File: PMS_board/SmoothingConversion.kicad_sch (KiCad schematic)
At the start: 0 parts

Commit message: add microcontroller pinout
fixed hotswap, added pinouts to microcontroller, and made notes for power smoothing
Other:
- note added: "100A fuse"
- note added: "12V Buck"
- note added: "Bulk Capacitors"
- note added: "In Rush Protection"
- note added: "Pi filter"
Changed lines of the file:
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@@
 	(generator_version "10.0")
 	(paper "A4")
+	(text "Pi filter"
+		(exclude_from_sim no)
+		(at 45.72 68.326 0)
+		(effects
+			(font
+				(size 1.27 1.27)
+			)
+		)
+	)
+	(text "Bulk Capacitors\n"
+		(exclude_from_sim no)
+		(at 49.53 63.246 0)
+		(effects
+			(font
+				(size 1.27 1.27)
+			)
+		)
+	)
+	(text "In Rush Protection\n"
+		(exclude_from_sim no)
+		(at 51.054 58.674 0)
+		(effects
+			(font
+				(size 1.27 1.27)
+			)
+		)
+	)
+	(text "12V Buck "
+		(exclude_from_sim no)
+		(at 46.99 72.898 0)
+		(effects
+			(font
+				(size 1.27 1.27)
+			)
+		)
+	)
+	(text "100A fuse\n"
+		(exclude_from_sim no)
+		(at 46.99 77.724 0)
+		(effects
+			(font
+				(size 1.27 1.27)
+			)
+		)
+	)
 )

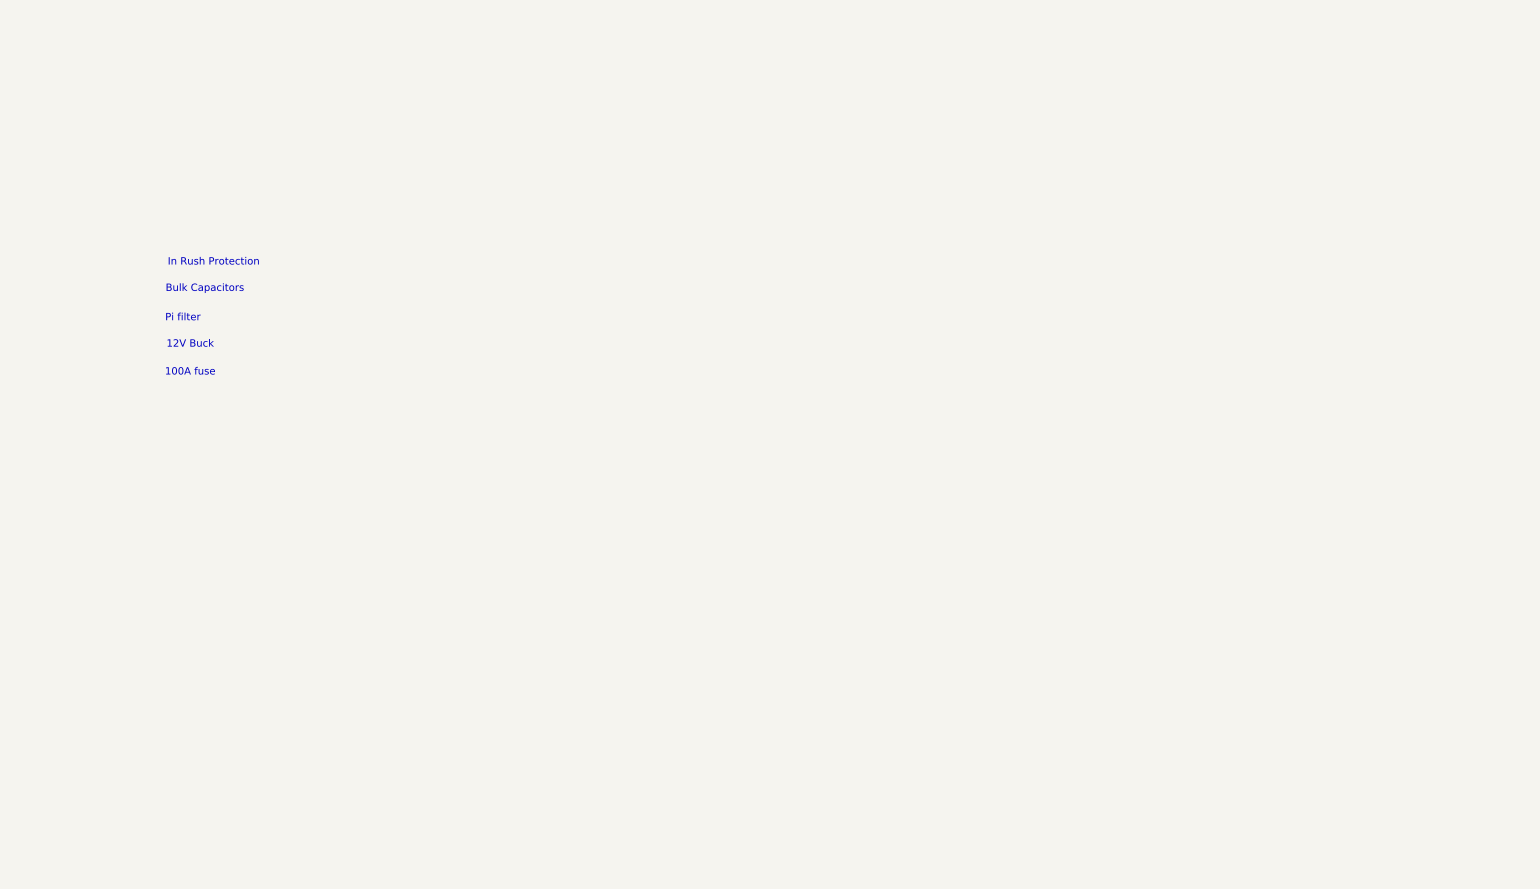
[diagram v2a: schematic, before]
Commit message: add power smoothing
I added the majority (i hope) of the necessary components for power smoothing and conversion. I also added notes to remind me and to inform others in my absence as to what still needs to be done to my knowledge.
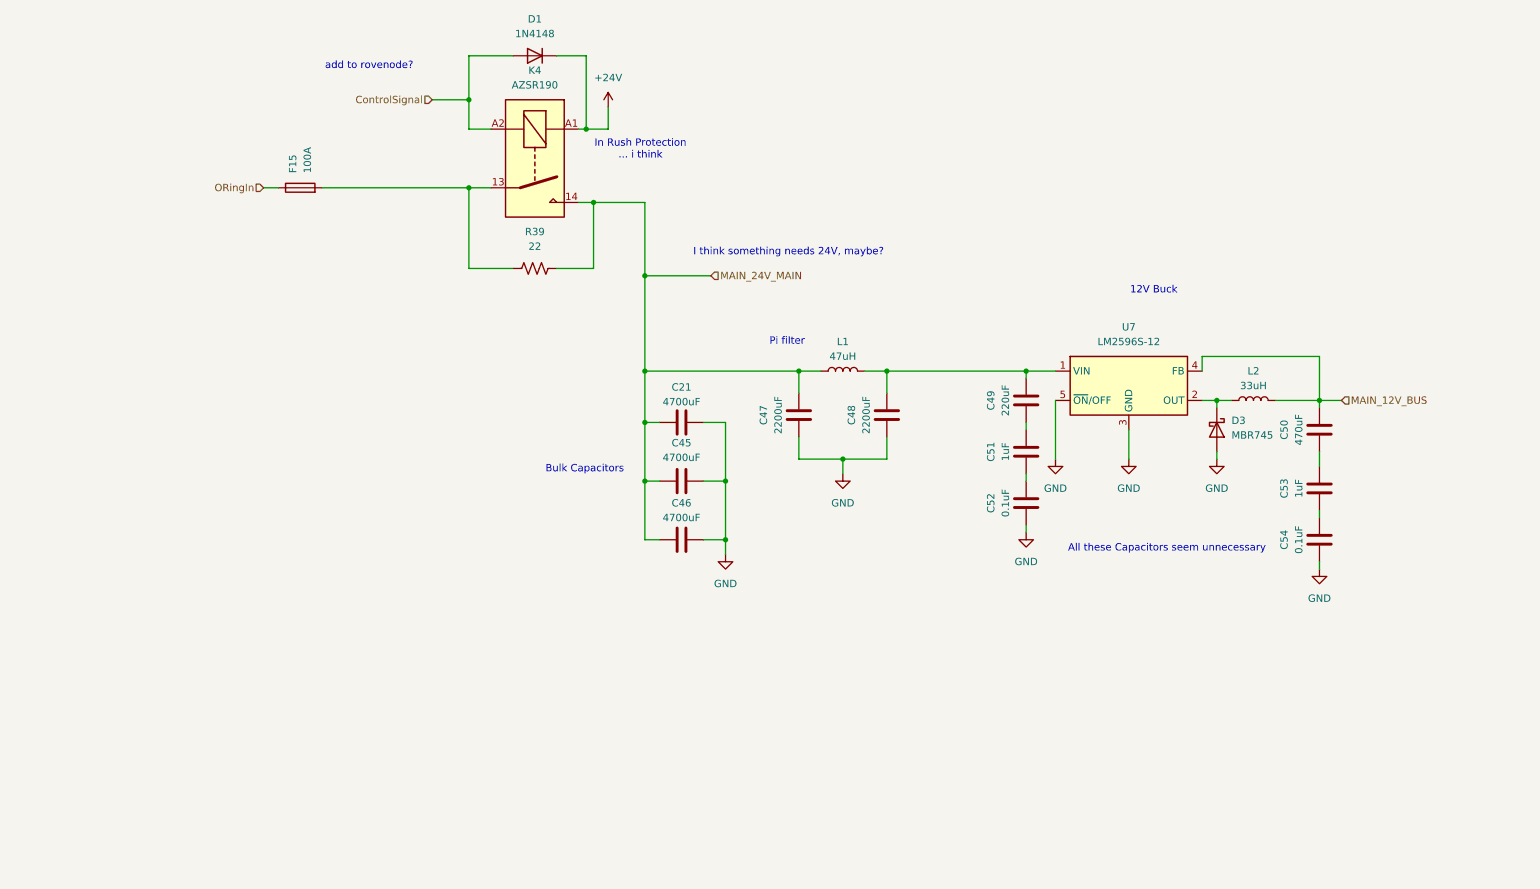
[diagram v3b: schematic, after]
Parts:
- added C21, C45, C46: 4700uF, symbol Device:C
- added C47, C48: 2200uF, symbol Device:C
- added C49: 220uF, symbol Device:C
- added C50: 470uF, symbol Device:C
- added C51, C53: 1uF, symbol Device:C
- added C52, C54: 0.1uF, symbol Device:C
- added D1: 1N4148, Diode_THT:D_DO-35_SOD27_P7.62mm_Horizontal, symbol Diode:1N4148
- added D3: MBR745, Package_TO_SOT_THT:TO-220-2_Vertical, symbol Diode:MBR745
- added F15: 100A, symbol Device:Fuse
- added K4: AZSR190, Relay_THT:Relay_SPST-NO_Fujitsu_FTR-LYAA005x_FormA_Vertical, symbol Relay:Relay_SPST-NO
- added L1: 47uH, symbol Device:L
- added L2: 33uH, symbol Device:L
- added R39: 22, symbol Device:R_US
- added U7: LM2596S-12, Package_TO_SOT_SMD:TO-263-5_TabPin3, symbol Regulator_Switching:LM2596S-12
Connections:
- new net: C50.2, C53.1
- new net: D3.1 (K), L2.1, U7.2 (OUT)
- new net: C53.2, C54.1
- new net: F15.2, K4.13, R39.2
- new net: C49.2, C51.1
- new net: C51.2, C52.1
- new net: C48.1, C49.1, L1.2, U7.1 (VIN)
- new net +24V: D1.1 (K), K4.A1
- new net ControlSignal: D1.2 (A), K4.A2
- new net GND: C21.1, C45.1, C46.1, C47.2, C48.2, C52.2, C54.2, D3.2 (A), U7.3 (GND), U7.5 (~{ON}/OFF)
- new net MAIN_12V_BUS: C50.1, L2.2, U7.4 (FB)
- new net MAIN_24V_MAIN: C21.2, C45.2, C46.2, C47.1, K4.14, L1.1, R39.1
- new net ORingIn: F15.1
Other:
- note added: "All these Capacitors seem unnecessary"
- note added: "I think something needs 24V, maybe?"
- note added: "In Rush Protection ... i think"
- note added: "add to rovenode?"
- note removed: "100A fuse"
- note removed: "In Rush Protection"

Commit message: add converter and friends
I added the converter symbols and updated the schematic. I chose the proper FETs and Diodes for ORing circuit.
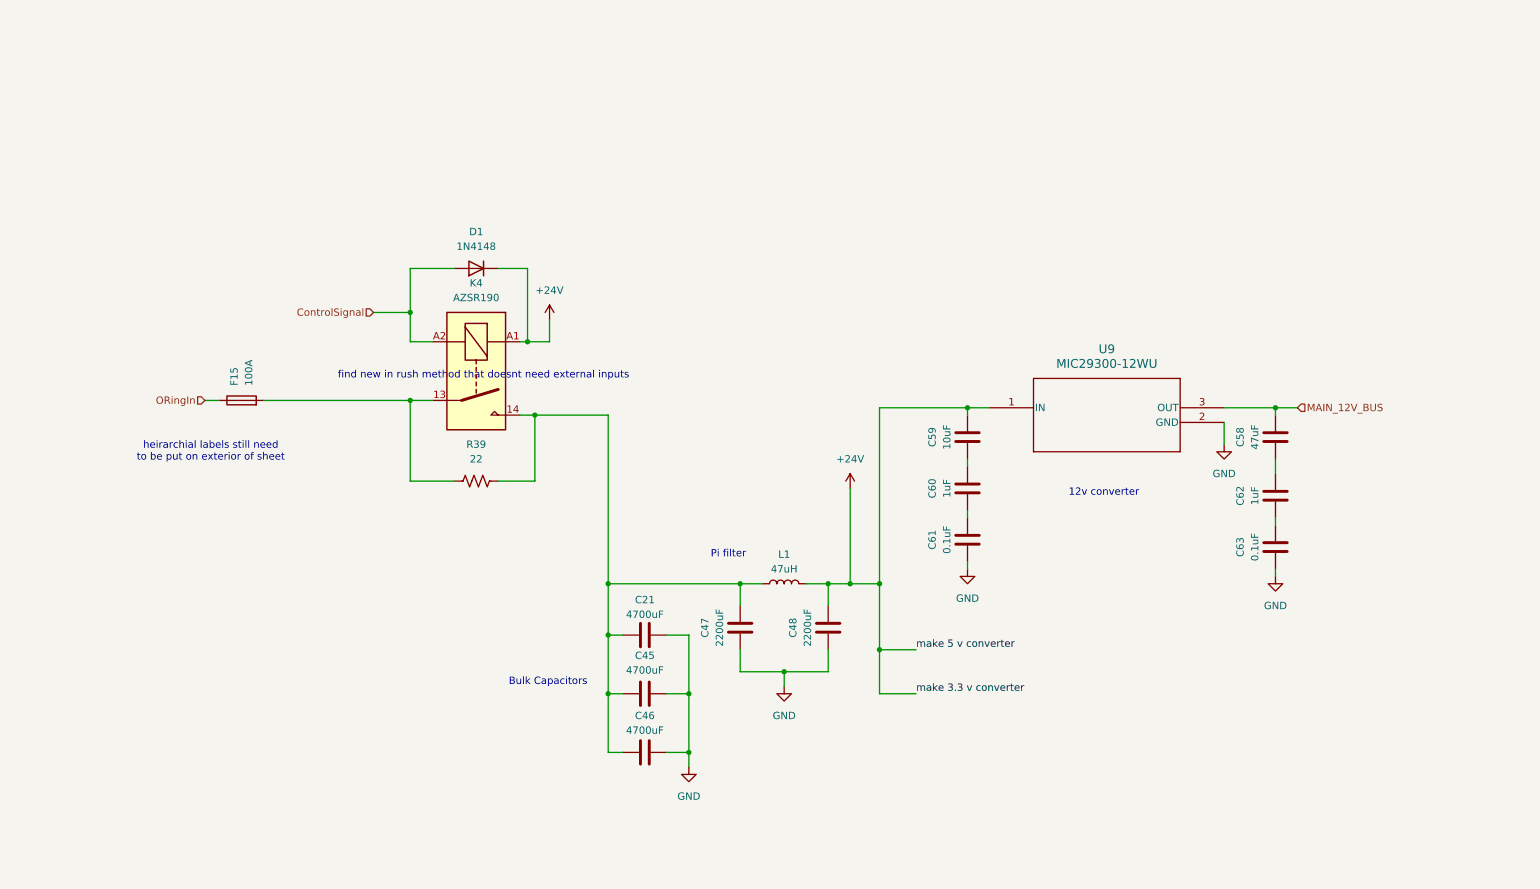
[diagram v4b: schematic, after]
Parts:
- removed C49: 220uF, symbol Device:C
- removed C50: 470uF, symbol Device:C
- removed C51, C53: 1uF, symbol Device:C
- removed C52, C54: 0.1uF, symbol Device:C
- removed D3: MBR745, Package_TO_SOT_THT:TO-220-2_Vertical, symbol Diode:MBR745
- removed L2: 33uH, symbol Device:L
- removed U7: LM2596S-12, Package_TO_SOT_SMD:TO-263-5_TabPin3, symbol Regulator_Switching:LM2596S-12
- added C58: 47uF, symbol Device:C
- added C59: 10uF, symbol Device:C
- added C60, C62: 1uF, symbol Device:C
- added C61, C63: 0.1uF, symbol Device:C
- added U9: MIC29300-12WU, TO220-3LD-PL-1_MCH, symbol MIC29300-12WU:MIC29300-12WU
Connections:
- net +24V: now also C48.1, L1.2, C59.1, U9.1 (IN)
- net GND: now also C61.2, C63.2, U9.2 (GND)
- net MAIN_12V_BUS: now also C58.1, U9.3 (OUT)
- net MAIN_24V_MAIN: no longer names the net of C21.2, C45.2, C46.2, C47.1, K4.14, L1.1, R39.1
- new net: C59.2, C60.1
- new net: C60.2, C61.1
- new net: C58.2, C62.1
- new net: C62.2, C63.1
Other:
- note added: "12v converter"
- note added: "find new in rush method that doesnt need external inputs"
- note added: "heirarchial labels still need to be put on exterior of sheet"
- note removed: "12V Buck"
- note removed: "All these Capacitors seem unnecessary"
- note removed: "I think something needs 24V, maybe?"
- note removed: "In Rush Protection ... i think"
- note removed: "add to rovenode?"
- moved on the sheet: C21, C45, C46, C47, C48, D1, F15, K4, L1, R39

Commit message: Add Bucks & Fix Issues
- Added 3V3 and 5V buck convertors
- Removed Pi filter
- adjusted capacitor values for Bulk Capacitors
- Added inrush protection to ORing circuit
- renamed various hierarchical pins for clarity
- renamed power rail pins due to naming conflicts
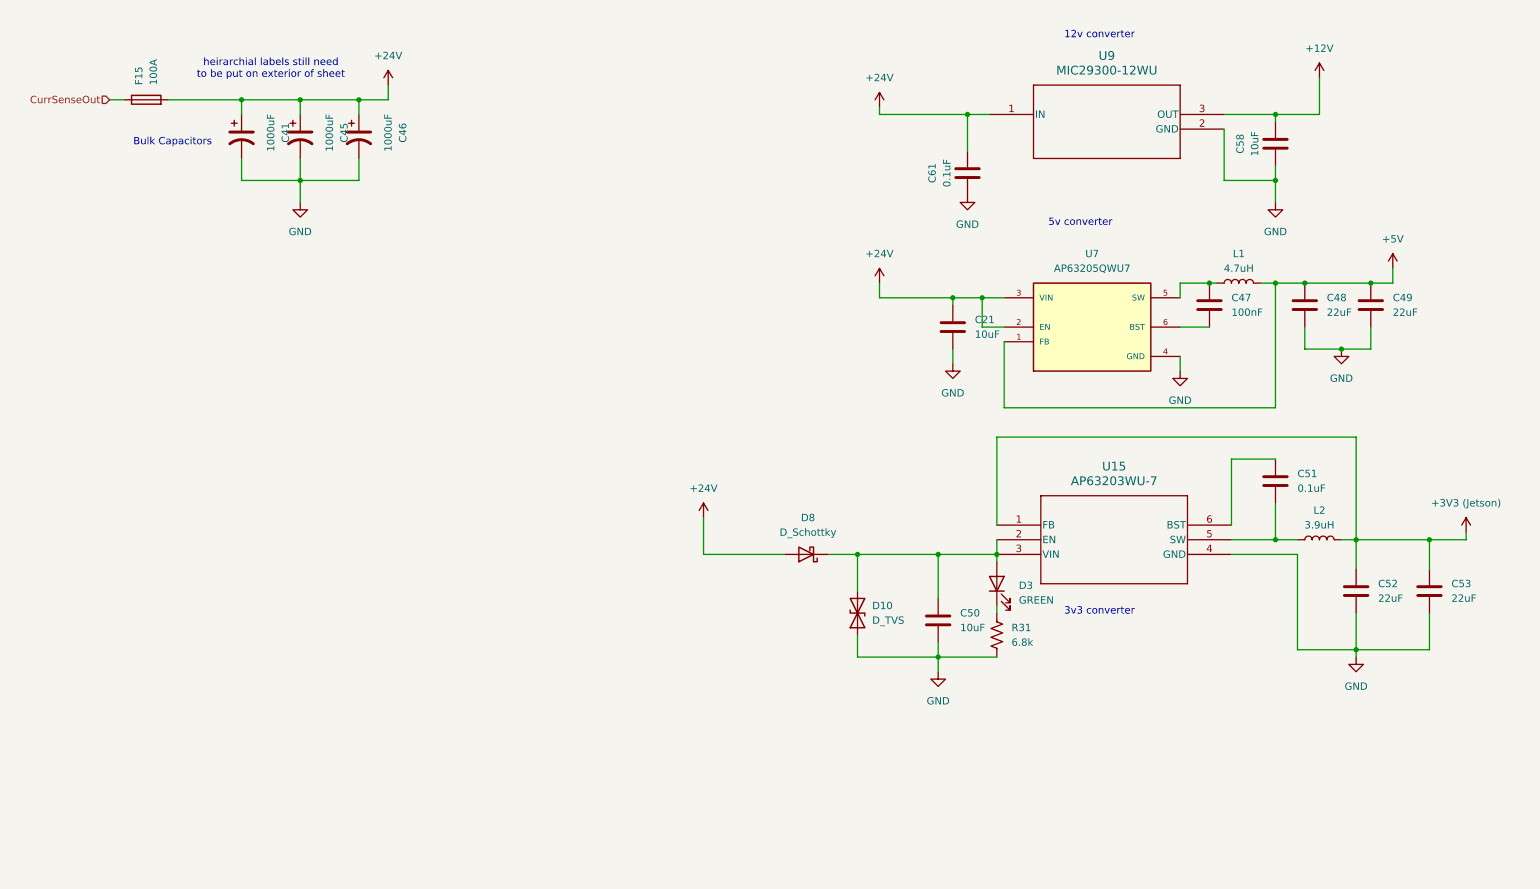
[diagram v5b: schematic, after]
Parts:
- removed C45, C46: 4700uF, symbol Device:C
- removed C59: 10uF, symbol Device:C
- removed C60, C62: 1uF, symbol Device:C
- removed C63: 0.1uF, symbol Device:C
- removed D1: 1N4148, Diode_THT:D_DO-35_SOD27_P7.62mm_Horizontal, symbol Diode:1N4148
- removed K4: AZSR190, Relay_THT:Relay_SPST-NO_Fujitsu_FTR-LYAA005x_FormA_Vertical, symbol Relay:Relay_SPST-NO
- removed R39: 22, symbol Device:R_US
- added C41, C45, C46: 1000uF, symbol Device:C_Polarized_US
- added C49: 22uF, Package_SO:SOIC-8_3.9x4.9mm_P1.27mm, symbol Device:C
- added C50: 10uF, Capacitor_SMD:C_0603_1608Metric_Pad1.08x0.95mm_HandSolder, symbol Device:C
- added C51: 0.1uF, Capacitor_SMD:C_0603_1608Metric_Pad1.08x0.95mm_HandSolder, symbol Device:C
- added C52, C53: 22uF, Capacitor_SMD:C_0603_1608Metric_Pad1.08x0.95mm_HandSolder, symbol Device:C
- added D10: D_TVS, Diode_SMD:D_SMA, symbol Device:D_TVS
- added D3: GREEN, LED_SMD:LED_0603_1608Metric_Pad1.05x0.95mm_HandSolder, symbol Device:LED
- added D8: D_Schottky, Diode_SMD:D_SOD-123F, symbol Device:D_Schottky
- added L2: 3.9uH, Inductor_SMD:L_1812_4532Metric_Pad1.30x3.40mm_HandSolder, symbol Device:L
- added R31: 6.8k, Resistor_SMD:R_0603_1608Metric_Pad0.98x0.95mm_HandSolder, symbol Device:R_US
- added U15: AP63203WU-7, SignalStack:AP63203WU-7_DIO, symbol AP63203WU-7:AP63203WU-7
- added U7: AP63205QWU7, AP63205QWU7:SOT95P280X100-6N, symbol AP63205QWU7:AP63205QWU7
- C21: value 4700uF -> 10uF; footprint (none) -> Package_SO:SOIC-8_3.9x4.9mm_P1.27mm
- C47: value 2200uF -> 100nF; footprint (none) -> Package_SO:SOIC-8_3.9x4.9mm_P1.27mm
- C48: value 2200uF -> 22uF; footprint (none) -> Package_SO:SOIC-8_3.9x4.9mm_P1.27mm
- C58: value 47uF -> 10uF
- L1: value 47uH -> 4.7uH; footprint (none) -> OptoDevice:Everlight_ITR9608-F
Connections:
- net +24V: now also C21.1, C61.1, F15.2, C41.1, C45.1, C46.1, D8.2 (A), U7.2 (EN), U7.3 (VIN); no longer C48.1, L1.2
- net GND: now also C21.2, C58.2, C41.2, C45.2, C46.2, C49.2, C50.2, C52.2, C53.2, D10.1 (A1), R31.1, U15.4 (GND), U7.4 (GND); no longer C21.1, C47.2
- net at C47.1, L1.1: now also U7.5 (SW); no longer C21.2
- net MAIN_12V_BUS renamed +12V
- net ORingIn renamed CurrSenseOut
- new net: C51.2, L2.1, U15.5 (SW)
- new net: C50.1, D10.2 (A2), D3.2 (A), D8.1 (K), U15.2 (EN), U15.3 (VIN)
- new net: C47.2, U7.6 (BST)
- new net: D3.1 (K), R31.2
- new net: C51.1, U15.6 (BST)
- new net +3V3 (Jetson): C52.1, C53.1, L2.2, U15.1 (FB)
- new net +5V: C48.1, C49.1, L1.2, U7.1 (FB)
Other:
- note added: "3v3 converter"
- note added: "5v converter"
- note removed: "Pi filter"
- note removed: "find new in rush method that doesnt need external inputs"
- moved on the sheet: C58, C61, F15, U9

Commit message: Finish Schematic
There's definitely stuff I missed, but I'm tired so we can review later. For my members to keep track of things, these are the changes/last minute additions I ran out of time to teach:
- brake chopper circuitry & reverse voltage protection for aux & motor rails
- microcontroller pinnouts
- net connections between sheets
- voltage resistors & system voltage measurements
- cell sense connectors & switch
- ADC routing
Please Please PLEASE ask questions about these additions. I don't want you guys to feel like you don't own this schematic, and I'm sorry I had to take away some of these designs to finish early. I definitely left too much on your plate to get everything perfect, which is my bad. I will happily walk through each and every circuit and help explain each part so you can better know your project when we get to reviewing and debugging later down the line.
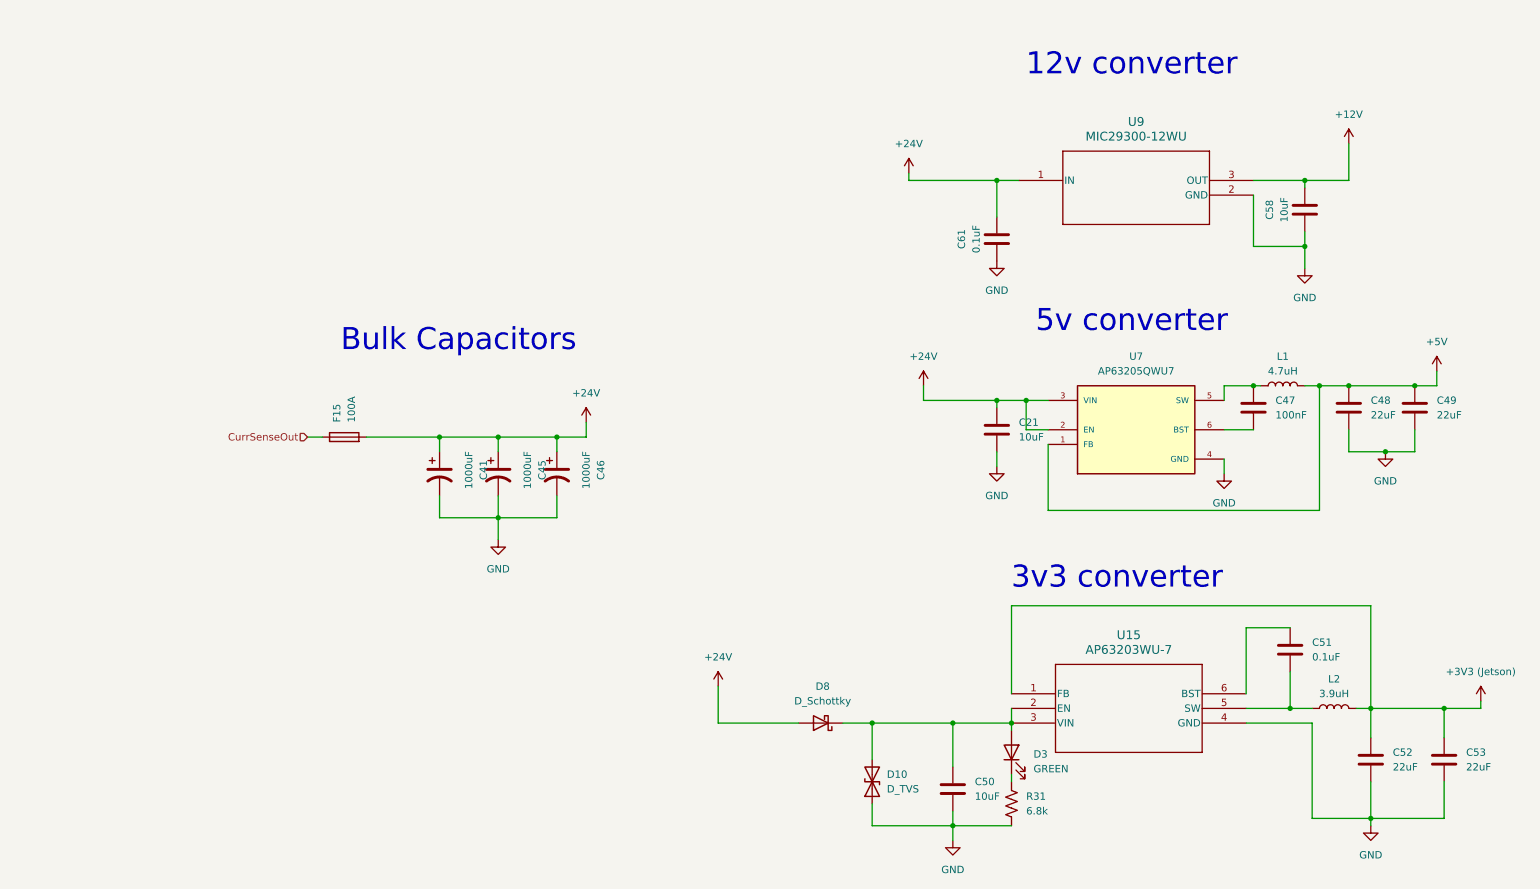
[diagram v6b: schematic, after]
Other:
- note removed: "heirarchial labels still need to be put on exterior of sheet"
- moved on the sheet: C21, C41, C45, C46, C47, C48, C49, C50, C51, C52, C53, C58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
